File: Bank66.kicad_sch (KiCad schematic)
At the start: 1 part, among them U1 XCKU5P-FFVB676

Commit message: finishing schematic
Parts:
- added R54: 240, Resistor_SMD:R_0201_0603Metric, symbol Device:R
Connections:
- net IO_L24P_T3U_N10_66_P: now reaches U1.B25 (IO_L24P_T3U_N10_66_P)
- net IO_L24N_T3U_N11_66_N: now reaches U1.B26 (IO_L24N_T3U_N11_66_N)
- net IO_L22N_T3U_N7_DBC_AD0N_66_N: now reaches U1.C24 (IO_L22N_T3U_N7_DBC_AD0N_66_N)
- net IO_L23N_T3U_N9_66_N: now reaches U1.C26 (IO_L23N_T3U_N9_66_N)
- net IO_L22P_T3U_N6_DBC_AD0P_66_P: now reaches U1.D23 (IO_L22P_T3U_N6_DBC_AD0P_66_P)
- net IO_L21P_T3L_N4_AD8P_66_P: now reaches U1.D24 (IO_L21P_T3L_N4_AD8P_66_P)
- net IO_L21N_T3L_N5_AD8N_66_N: now reaches U1.D25 (IO_L21N_T3L_N5_AD8N_66_N)
- net IO_L23P_T3U_N8_66_P: now reaches U1.D26 (IO_L23P_T3U_N8_66_P)
- net IO_L20N_T3L_N3_AD1N_66_N: now reaches U1.E23 (IO_L20N_T3L_N3_AD1N_66_N)
- net IO_L19P_T3L_N0_DBC_AD9P_66_P: now reaches U1.E25 (IO_L19P_T3L_N0_DBC_AD9P_66_P)
- net IO_L19N_T3L_N1_DBC_AD9N_66_N: now reaches U1.E26 (IO_L19N_T3L_N1_DBC_AD9N_66_N)
- net IO_T3U_N12_66: now reaches U1.F22 (IO_T3U_N12_66)
- net IO_L20P_T3L_N2_AD1P_66_P: now reaches U1.F23 (IO_L20P_T3L_N2_AD1P_66_P)
- net IO_L16P_T2U_N6_QBC_AD3P_66_P: now reaches U1.F24 (IO_L16P_T2U_N6_QBC_AD3P_66_P)
- net IO_L16N_T2U_N7_QBC_AD3N_66_N: now reaches U1.F25 (IO_L16N_T2U_N7_QBC_AD3N_66_N)
- net IO_T2U_N12_66: now reaches U1.G22 (IO_T2U_N12_66)
- net IO_L13P_T2L_N0_GC_QBC_66_P: now reaches U1.G24 (IO_L13P_T2L_N0_GC_QBC_66_P)
- net IO_L13N_T2L_N1_GC_QBC_66_N: now reaches U1.G25 (IO_L13N_T2L_N1_GC_QBC_66_N)
- net IO_L17N_T2U_N9_AD10N_66_N: now reaches U1.G26 (IO_L17N_T2U_N9_AD10N_66_N)
- net IO_L18P_T2U_N10_AD2P_66_P: now reaches U1.H21 (IO_L18P_T2U_N10_AD2P_66_P)
- net IO_L18N_T2U_N11_AD2N_66_N: now reaches U1.H22 (IO_L18N_T2U_N11_AD2N_66_N)
- net IO_L14P_T2L_N2_GC_66_P: now reaches U1.H23 (IO_L14P_T2L_N2_GC_66_P)
- net IO_L14N_T2L_N3_GC_66_N: now reaches U1.H24 (IO_L14N_T2L_N3_GC_66_N)
- net IO_L17P_T2U_N8_AD10P_66_P: now reaches U1.H26 (IO_L17P_T2U_N8_AD10P_66_P)
- net IO_L3P_T0L_N4_AD15P_66_P: now reaches U1.J19 (IO_L3P_T0L_N4_AD15P_66_P)
- net IO_L3N_T0L_N5_AD15N_66_N: now reaches U1.J20 (IO_L3N_T0L_N5_AD15N_66_N)
- net IO_L5N_T0U_N9_AD14N_66_N: now reaches U1.J21 (IO_L5N_T0U_N9_AD14N_66_N)
- net IO_L12P_T1U_N10_GC_66_P: now reaches U1.J23 (IO_L12P_T1U_N10_GC_66_P)
- net IO_L12N_T1U_N11_GC_66_N: now reaches U1.J24 (IO_L12N_T1U_N11_GC_66_N)
- net IO_L15P_T2L_N4_AD11P_66_P: now reaches U1.J25 (IO_L15P_T2L_N4_AD11P_66_P)
- net IO_L15N_T2L_N5_AD11N_66_N: now reaches U1.J26 (IO_L15N_T2L_N5_AD11N_66_N)
- net IO_L1N_T0L_N1_DBC_66_N: now reaches U1.K18 (IO_L1N_T0L_N1_DBC_66_N)
- net IO_L6N_T0U_N11_AD6N_66_N: now reaches U1.K20 (IO_L6N_T0U_N11_AD6N_66_N)
- net IO_L5P_T0U_N8_AD14P_66_P: now reaches U1.K21 (IO_L5P_T0U_N8_AD14P_66_P)
- net IO_L11P_T1U_N8_GC_66_P: now reaches U1.K22 (IO_L11P_T1U_N8_GC_66_P)
- net IO_L11N_T1U_N9_GC_66_N: now reaches U1.K23 (IO_L11N_T1U_N9_GC_66_N)
- net IO_L9P_T1L_N4_AD12P_66_P: now reaches U1.K25 (IO_L9P_T1L_N4_AD12P_66_P)
- net IO_L9N_T1L_N5_AD12N_66_N: now reaches U1.K26 (IO_L9N_T1L_N5_AD12N_66_N)
- net IO_L1P_T0L_N0_DBC_66_P: now reaches U1.L18 (IO_L1P_T0L_N0_DBC_66_P)
- net IO_L4N_T0U_N7_DBC_AD7N_66_N: now reaches U1.L19 (IO_L4N_T0U_N7_DBC_AD7N_66_N)
- net IO_L6P_T0U_N10_AD6P_66_P: now reaches U1.L20 (IO_L6P_T0U_N10_AD6P_66_P)
- net IO_L7P_T1L_N0_QBC_AD13P_66_P: now reaches U1.L22 (IO_L7P_T1L_N0_QBC_AD13P_66_P)
- net IO_L7N_T1L_N1_QBC_AD13N_66_N: now reaches U1.L23 (IO_L7N_T1L_N1_QBC_AD13N_66_N)
- net IO_L10P_T1U_N6_QBC_AD4P_66_P: now reaches U1.L24 (IO_L10P_T1U_N6_QBC_AD4P_66_P)
- net IO_L10N_T1U_N7_QBC_AD4N_66_N: now reaches U1.L25 (IO_L10N_T1U_N7_QBC_AD4N_66_N)
- net IO_L4P_T0U_N6_DBC_AD7P_66_P: now reaches U1.M19 (IO_L4P_T0U_N6_DBC_AD7P_66_P)
- net IO_L2P_T0L_N2_66_P: now reaches U1.M20 (IO_L2P_T0L_N2_66_P)
- net IO_L2N_T0L_N3_66_N: now reaches U1.M21 (IO_L2N_T0L_N3_66_N)
- net VRP: now reaches U1.M22 (IO_T0U_N12_VRP_66)
- net VRP: now also R54.1
- net IO_T1U_N12_66: now reaches U1.M24 (IO_T1U_N12_66)
- net IO_L8P_T1L_N2_AD5P_66_P: now reaches U1.M25 (IO_L8P_T1L_N2_AD5P_66_P)
- net IO_L8N_T1L_N3_AD5N_66_N: now reaches U1.M26 (IO_L8N_T1L_N3_AD5N_66_N)
- new net GND: R54.2

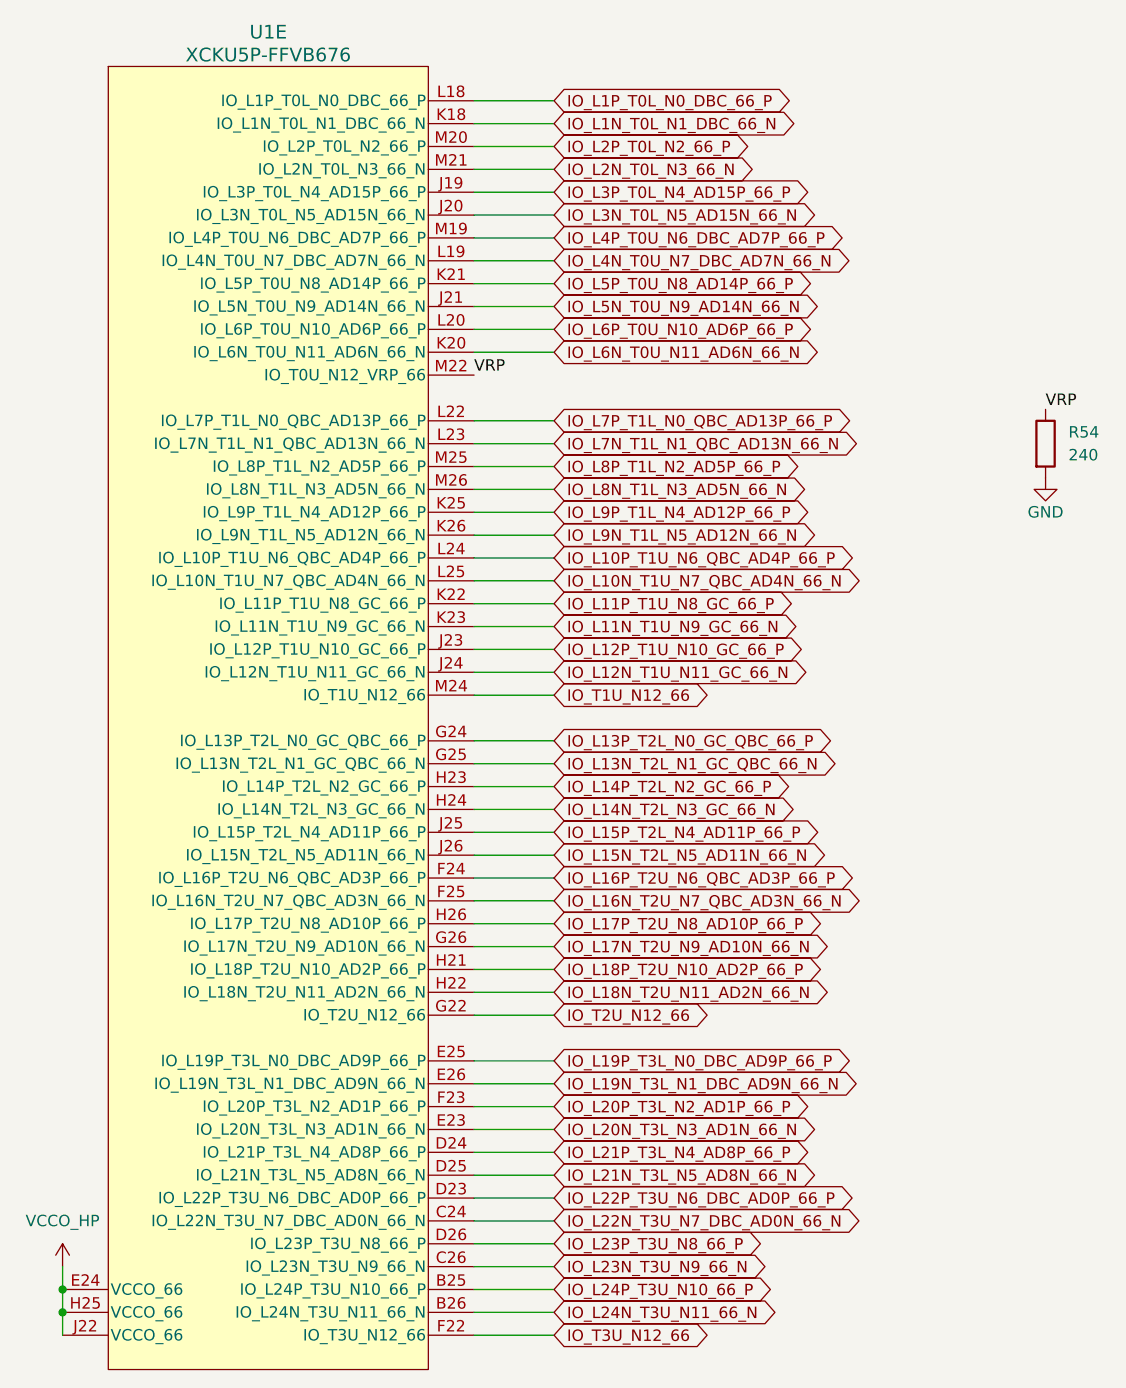
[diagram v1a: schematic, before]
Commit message: change net name to of IO diff pairs, add a scripts for name modification
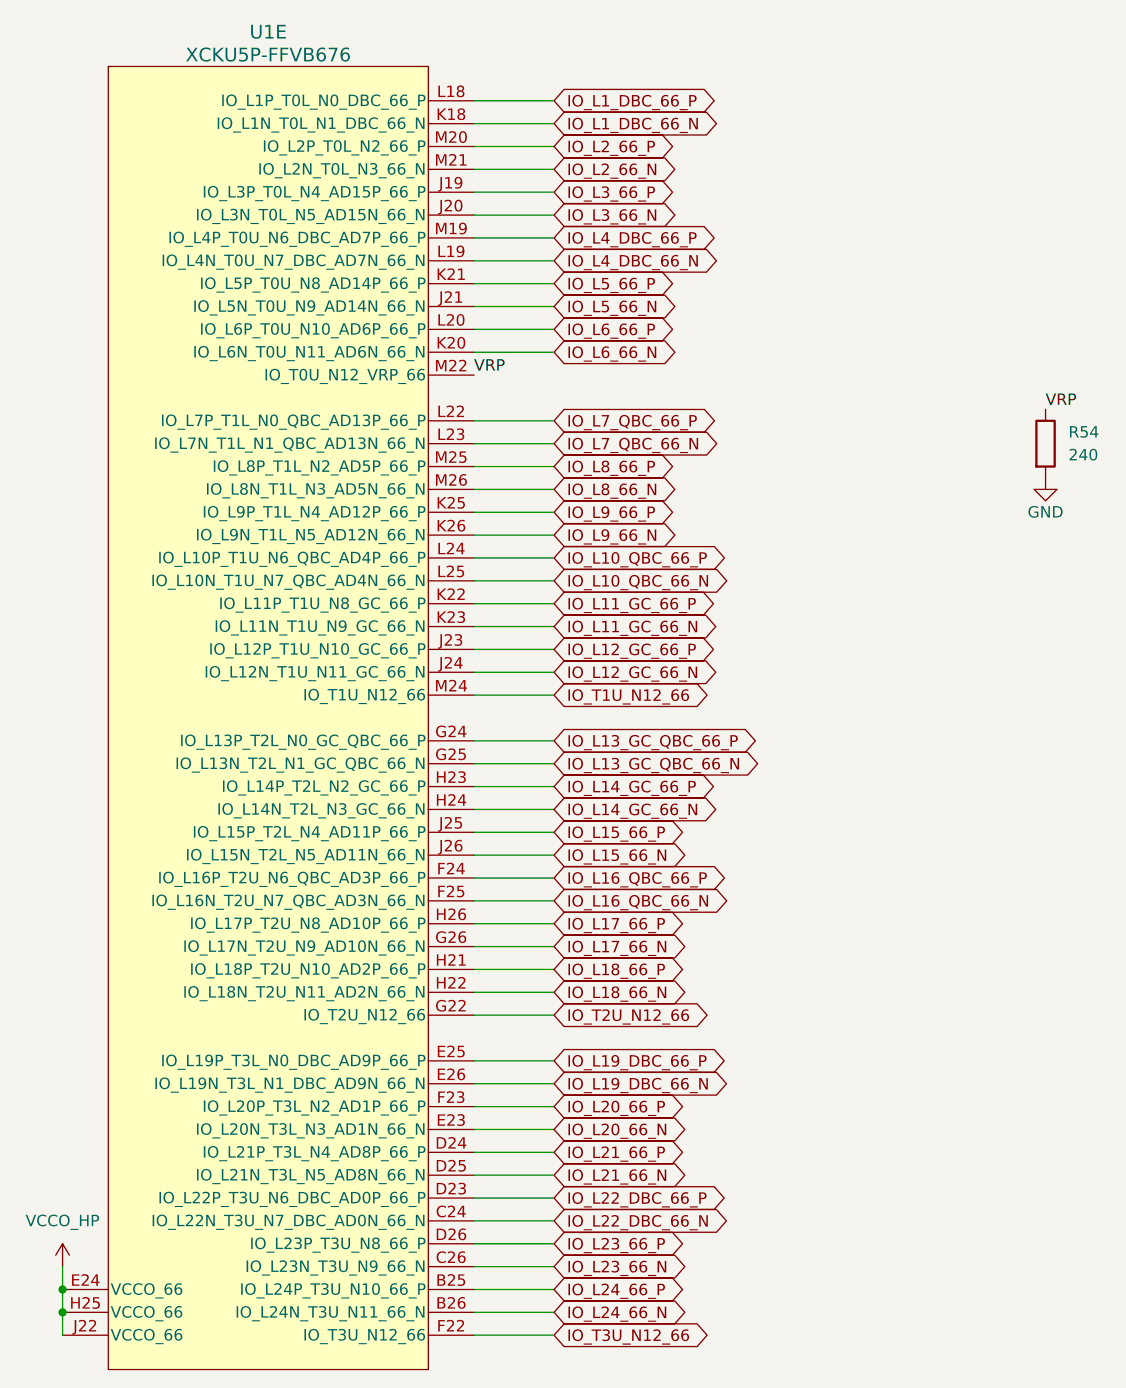
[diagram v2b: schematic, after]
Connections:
- net IO_L10N_T1U_N7_QBC_AD4N_66_N renamed IO_L10_QBC_66_N
- net IO_L10P_T1U_N6_QBC_AD4P_66_P renamed IO_L10_QBC_66_P
- net IO_L11N_T1U_N9_GC_66_N renamed IO_L11_GC_66_N
- net IO_L11P_T1U_N8_GC_66_P renamed IO_L11_GC_66_P
- net IO_L12N_T1U_N11_GC_66_N renamed IO_L12_GC_66_N
- net IO_L12P_T1U_N10_GC_66_P renamed IO_L12_GC_66_P
- net IO_L13N_T2L_N1_GC_QBC_66_N renamed IO_L13_GC_QBC_66_N
- net IO_L13P_T2L_N0_GC_QBC_66_P renamed IO_L13_GC_QBC_66_P
- net IO_L14N_T2L_N3_GC_66_N renamed IO_L14_GC_66_N
- net IO_L14P_T2L_N2_GC_66_P renamed IO_L14_GC_66_P
- net IO_L15N_T2L_N5_AD11N_66_N renamed IO_L15_66_N
- net IO_L15P_T2L_N4_AD11P_66_P renamed IO_L15_66_P
- net IO_L16N_T2U_N7_QBC_AD3N_66_N renamed IO_L16_QBC_66_N
- net IO_L16P_T2U_N6_QBC_AD3P_66_P renamed IO_L16_QBC_66_P
- net IO_L17N_T2U_N9_AD10N_66_N renamed IO_L17_66_N
- net IO_L17P_T2U_N8_AD10P_66_P renamed IO_L17_66_P
- net IO_L18N_T2U_N11_AD2N_66_N renamed IO_L18_66_N
- net IO_L18P_T2U_N10_AD2P_66_P renamed IO_L18_66_P
- net IO_L19N_T3L_N1_DBC_AD9N_66_N renamed IO_L19_DBC_66_N
- net IO_L19P_T3L_N0_DBC_AD9P_66_P renamed IO_L19_DBC_66_P
- net IO_L1N_T0L_N1_DBC_66_N renamed IO_L1_DBC_66_N
- net IO_L1P_T0L_N0_DBC_66_P renamed IO_L1_DBC_66_P
- net IO_L20N_T3L_N3_AD1N_66_N renamed IO_L20_66_N
- net IO_L20P_T3L_N2_AD1P_66_P renamed IO_L20_66_P
- net IO_L21N_T3L_N5_AD8N_66_N renamed IO_L21_66_N
- net IO_L21P_T3L_N4_AD8P_66_P renamed IO_L21_66_P
- net IO_L22N_T3U_N7_DBC_AD0N_66_N renamed IO_L22_DBC_66_N
- net IO_L22P_T3U_N6_DBC_AD0P_66_P renamed IO_L22_DBC_66_P
- net IO_L23N_T3U_N9_66_N renamed IO_L23_66_N
- net IO_L23P_T3U_N8_66_P renamed IO_L23_66_P
- net IO_L24N_T3U_N11_66_N renamed IO_L24_66_N
- net IO_L24P_T3U_N10_66_P renamed IO_L24_66_P
- net IO_L2N_T0L_N3_66_N renamed IO_L2_66_N
- net IO_L2P_T0L_N2_66_P renamed IO_L2_66_P
- net IO_L3N_T0L_N5_AD15N_66_N renamed IO_L3_66_N
- net IO_L3P_T0L_N4_AD15P_66_P renamed IO_L3_66_P
- net IO_L4N_T0U_N7_DBC_AD7N_66_N renamed IO_L4_DBC_66_N
- net IO_L4P_T0U_N6_DBC_AD7P_66_P renamed IO_L4_DBC_66_P
- net IO_L5N_T0U_N9_AD14N_66_N renamed IO_L5_66_N
- net IO_L5P_T0U_N8_AD14P_66_P renamed IO_L5_66_P
- net IO_L6N_T0U_N11_AD6N_66_N renamed IO_L6_66_N
- net IO_L6P_T0U_N10_AD6P_66_P renamed IO_L6_66_P
- net IO_L7N_T1L_N1_QBC_AD13N_66_N renamed IO_L7_QBC_66_N
- net IO_L7P_T1L_N0_QBC_AD13P_66_P renamed IO_L7_QBC_66_P
- net IO_L8N_T1L_N3_AD5N_66_N renamed IO_L8_66_N
- net IO_L8P_T1L_N2_AD5P_66_P renamed IO_L8_66_P
- net IO_L9N_T1L_N5_AD12N_66_N renamed IO_L9_66_N
- net IO_L9P_T1L_N4_AD12P_66_P renamed IO_L9_66_P
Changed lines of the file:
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@@
 		)
 	)
-	(global_label "IO_L19P_T3L_N0_DBC_AD9P_66_P"
+	(global_label "IO_L19_DBC_66_P"
 		(shape bidirectional)
 		(at 111.76 138.43 0)
@@
 		)
 	)
-	(global_label "IO_L7N_T1L_N1_QBC_AD13N_66_N"
+	(global_label "IO_L7_QBC_66_N"
 		(shape bidirectional)
 		(at 111.76 69.85 0)
@@
 		)
 	)
-	(global_label "IO_L15P_T2L_N4_AD11P_66_P"
+	(global_label "IO_L15_66_P"
 		(shape bidirectional)
 		(at 111.76 113.03 0)
@@
 		)
 	)
-	(global_label "IO_L2N_T0L_N3_66_N"
+	(global_label "IO_L2_66_N"
 		(shape bidirectional)
 		(at 111.76 39.37 0)
@@
 		)
 	)
-	(global_label "IO_L12P_T1U_N10_GC_66_P"
+	(global_label "IO_L12_GC_66_P"
 		(shape bidirectional)
 		(at 111.76 92.71 0)
@@
 		)
 	)
-	(global_label "IO_L5P_T0U_N8_AD14P_66_P"
+	(global_label "IO_L5_66_P"
 		(shape bidirectional)
 		(at 111.76 52.07 0)
@@
 		)
 	)
-	(global_label "IO_L6P_T0U_N10_AD6P_66_P"
+	(global_label "IO_L6_66_P"
 		(shape bidirectional)
 		(at 111.76 57.15 0)
@@
 		)
 	)
-	(global_label "IO_L5N_T0U_N9_AD14N_66_N"
+	(global_label "IO_L5_66_N"
 		(shape bidirectional)
 		(at 111.76 54.61 0)
@@
 		)
 	)
-	(global_label "IO_L17P_T2U_N8_AD10P_66_P"
+	(global_label "IO_L17_66_P"
 		(shape bidirectional)
 		(at 111.76 123.19 0)
@@
 		)
 	)
-	(global_label "IO_L8P_T1L_N2_AD5P_66_P"
+	(global_label "IO_L8_66_P"
 		(shape bidirectional)
 		(at 111.76 72.39 0)
@@
 		)
 	)
-	(global_label "IO_L4N_T0U_N7_DBC_AD7N_66_N"
+	(global_label "IO_L4_DBC_66_N"
 		(shape bidirectional)
 		(at 111.76 49.53 0)
@@
 		)
 	)
-	(global_label "IO_L7P_T1L_N0_QBC_AD13P_66_P"
+	(global_label "IO_L7_QBC_66_P"
 		(shape bidirectional)
 		(at 111.76 67.31 0)
@@
 		)
 	)
-	(global_label "IO_L11N_T1U_N9_GC_66_N"
+	(global_label "IO_L11_GC_66_N"
 		(shape bidirectional)
 		(at 111.76 90.17 0)
@@
 		)
 	)
-	(global_label "IO_L22P_T3U_N6_DBC_AD0P_66_P"
+	(global_label "IO_L22_DBC_66_P"
 		(shape bidirectional)
 		(at 111.76 153.67 0)
@@
 		)
 	)
-	(global_label "IO_L3N_T0L_N5_AD15N_66_N"
+	(global_label "IO_L3_66_N"
 		(shape bidirectional)
 		(at 111.76 44.45 0)
@@
 		)
 	)
-	(global_label "IO_L13N_T2L_N1_GC_QBC_66_N"
+	(global_label "IO_L13_GC_QBC_66_N"
 		(shape bidirectional)
 		(at 111.76 105.41 0)
@@
 		)
 	)
-	(global_label "IO_L22N_T3U_N7_DBC_AD0N_66_N"
+	(global_label "IO_L22_DBC_66_N"
 		(shape bidirectional)
 		(at 111.76 156.21 0)
@@
 		)
 	)
-	(global_label "IO_L10P_T1U_N6_QBC_AD4P_66_P"
+	(global_label "IO_L10_QBC_66_P"
 		(shape bidirectional)
 		(at 111.76 82.55 0)
@@
 		)
 	)
-	(global_label "IO_L4P_T0U_N6_DBC_AD7P_66_P"
+	(global_label "IO_L4_DBC_66_P"
 		(shape bidirectional)
 		(at 111.76 46.99 0)
@@
 		)
 	)
-	(global_label "IO_L12N_T1U_N11_GC_66_N"
+	(global_label "IO_L12_GC_66_N"
 		(shape bidirectional)
 		(at 111.76 95.25 0)
@@
 		)
 	)
-	(global_label "IO_L20P_T3L_N2_AD1P_66_P"
+	(global_label "IO_L20_66_P"
 		(shape bidirectional)
 		(at 111.76 143.51 0)
@@
 		)
 	)
-	(global_label "IO_L18N_T2U_N11_AD2N_66_N"
+	(global_label "IO_L18_66_N"
 		(shape bidirectional)
 		(at 111.76 130.81 0)
@@
 		)
 	)
-	(global_label "IO_L15N_T2L_N5_AD11N_66_N"
+	(global_label "IO_L15_66_N"
 		(shape bidirectional)
 		(at 111.76 115.57 0)
@@
 		)
 	)
-	(global_label "IO_L19N_T3L_N1_DBC_AD9N_66_N"
+	(global_label "IO_L19_DBC_66_N"
 		(shape bidirectional)
 		(at 111.76 140.97 0)
@@
 		)
 	)
-	(global_label "IO_L24P_T3U_N10_66_P"
+	(global_label "IO_L24_66_P"
 		(shape bidirectional)
 		(at 111.76 163.83 0)
@@
 		)
 	)
-	(global_label "IO_L8N_T1L_N3_AD5N_66_N"
+	(global_label "IO_L8_66_N"
 		(shape bidirectional)
 		(at 111.76 74.93 0)
@@
 		)
 	)
-	(global_label "IO_L10N_T1U_N7_QBC_AD4N_66_N"
+	(global_label "IO_L10_QBC_66_N"
 		(shape bidirectional)
 		(at 111.76 85.09 0)
@@
 		)
 	)
-	(global_label "IO_L20N_T3L_N3_AD1N_66_N"
+	(global_label "IO_L20_66_N"
 		(shape bidirectional)
 		(at 111.76 146.05 0)
@@
 		)
 	)
-	(global_label "IO_L16N_T2U_N7_QBC_AD3N_66_N"
+	(global_label "IO_L16_QBC_66_N"
 		(shape bidirectional)
 		(at 111.76 120.65 0)
@@
 		)
 	)
-	(global_label "IO_L24N_T3U_N11_66_N"
+	(global_label "IO_L24_66_N"
 		(shape bidirectional)
 		(at 111.76 166.37 0)
@@
 		)
 	)
-	(global_label "IO_L14P_T2L_N2_GC_66_P"
+	(global_label "IO_L14_GC_66_P"
 		(shape bidirectional)
 		(at 111.76 107.95 0)
@@
 		)
 	)
-	(global_label "IO_L16P_T2U_N6_QBC_AD3P_66_P"
+	(global_label "IO_L16_QBC_66_P"
 		(shape bidirectional)
 		(at 111.76 118.11 0)
@@
 		)
 	)
-	(global_label "IO_L1P_T0L_N0_DBC_66_P"
+	(global_label "IO_L1_DBC_66_P"
 		(shape bidirectional)
 		(at 111.76 31.75 0)
@@
 		)
 	)
-	(global_label "IO_L9P_T1L_N4_AD12P_66_P"
+	(global_label "IO_L9_66_P"
 		(shape bidirectional)
 		(at 111.76 77.47 0)
@@
 		)
 	)
-	(global_label "IO_L1N_T0L_N1_DBC_66_N"
+	(global_label "IO_L1_DBC_66_N"
 		(shape bidirectional)
 		(at 111.76 34.29 0)
@@
 		)
 	)
-	(global_label "IO_L2P_T0L_N2_66_P"
+	(global_label "IO_L2_66_P"
 		(shape bidirectional)
 		(at 111.76 36.83 0)
@@
 		)
 	)
-	(global_label "IO_L23P_T3U_N8_66_P"
+	(global_label "IO_L23_66_P"
 		(shape bidirectional)
 		(at 111.76 158.75 0)
@@
 		)
 	)
-	(global_label "IO_L23N_T3U_N9_66_N"
+	(global_label "IO_L23_66_N"
 		(shape bidirectional)
 		(at 111.76 161.29 0)
@@
 		)
 	)
-	(global_label "IO_L21N_T3L_N5_AD8N_66_N"
+	(global_label "IO_L21_66_N"
 		(shape bidirectional)
 		(at 111.76 151.13 0)
@@
 		)
 	)
-	(global_label "IO_L6N_T0U_N11_AD6N_66_N"
+	(global_label "IO_L6_66_N"
 		(shape bidirectional)
 		(at 111.76 59.69 0)
@@
 		)
 	)
-	(global_label "IO_L13P_T2L_N0_GC_QBC_66_P"
+	(global_label "IO_L13_GC_QBC_66_P"
 		(shape bidirectional)
 		(at 111.76 102.87 0)
@@
 		)
 	)
-	(global_label "IO_L17N_T2U_N9_AD10N_66_N"
+	(global_label "IO_L17_66_N"
 		(shape bidirectional)
 		(at 111.76 125.73 0)
@@
 		)
 	)
-	(global_label "IO_L3P_T0L_N4_AD15P_66_P"
+	(global_label "IO_L3_66_P"
 		(shape bidirectional)
 		(at 111.76 41.91 0)
@@
 		)
 	)
-	(global_label "IO_L11P_T1U_N8_GC_66_P"
+	(global_label "IO_L11_GC_66_P"
 		(shape bidirectional)
 		(at 111.76 87.63 0)
@@
 		)
 	)
-	(global_label "IO_L18P_T2U_N10_AD2P_66_P"
+	(global_label "IO_L18_66_P"
 		(shape bidirectional)
 		(at 111.76 128.27 0)
@@
 		)
 	)
-	(global_label "IO_L14N_T2L_N3_GC_66_N"
+	(global_label "IO_L14_GC_66_N"
 		(shape bidirectional)
 		(at 111.76 110.49 0)
@@
 		)
 	)
-	(global_label "IO_L9N_T1L_N5_AD12N_66_N"
+	(global_label "IO_L9_66_N"
 		(shape bidirectional)
 		(at 111.76 80.01 0)
@@
 		)
 	)
-	(global_label "IO_L21P_T3L_N4_AD8P_66_P"
+	(global_label "IO_L21_66_P"
 		(shape bidirectional)
 		(at 111.76 148.59 0)
